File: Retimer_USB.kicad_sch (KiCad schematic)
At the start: 16 parts, among them IC1 PI2EQX22024XEAEX

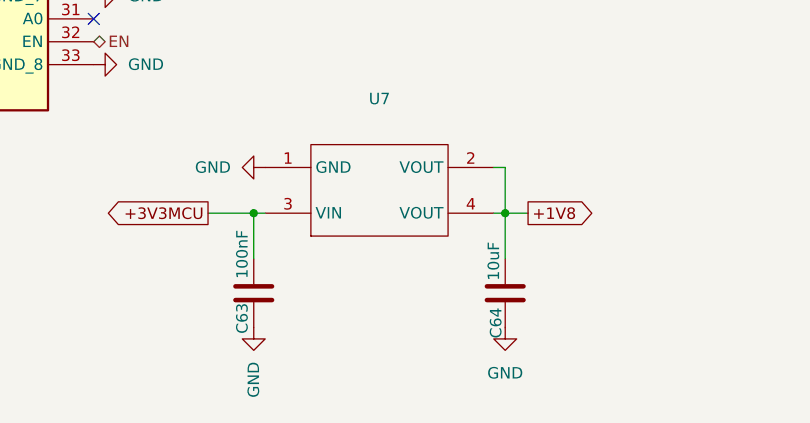
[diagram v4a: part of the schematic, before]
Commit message: added proper capacitators for ldo
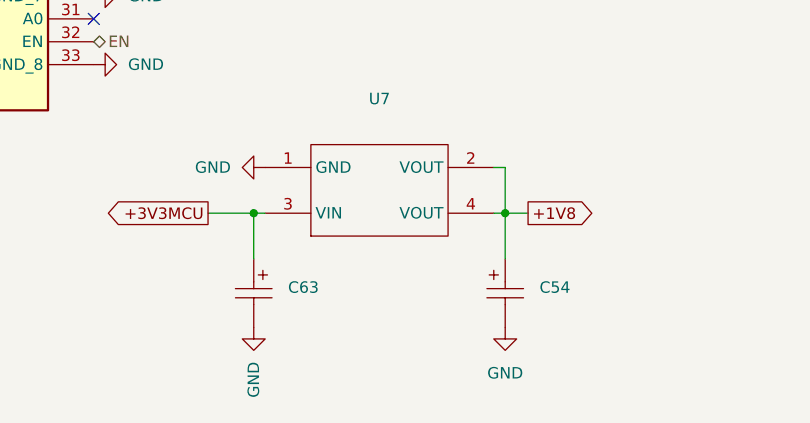
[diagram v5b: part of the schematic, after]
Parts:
- removed C63: 100nF, Capacitor_SMD:C_0201_0603Metric, symbol Device:C
- removed C64: 10uF, Capacitor_SMD:C_0603_1608Metric, symbol Device:C
- added C54: 10uF, TAJA106K016RNJ:CAP-SMD_L3.2-W1.6-RD-C7171, symbol TAJA106K016RNJ:TAJA106K016RNJ
- added C63: 100nF, TAJA104K035RNJ:CASE-A_3216, symbol TAJA104K035RNJ:TAJA104K035RNJ
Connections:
- net +1V8: now also C54.1
- net +3V3MCU: now also C63.1
- net GND: now also C54.2, C63.2
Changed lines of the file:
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@@
+	)
+	(symbol
+		(lib_id "TAJA104K035RNJ:TAJA104K035RNJ")
+		(at 198.12 133.35 270)
+		(unit 1)
+		(exclude_from_sim no)
+		(in_bom yes)
+		(on_board yes)
+		(dnp no)
+		(fields_autoplaced yes)
+		(property "Reference" "C63"
+			(at 201.93 132.7149 90)
+			(effects
+				(font
+					(size 1.27 1.27)
+				)
+				(justify left)
+			)
+		)
+		(property "Value" "100nF"
+			(at 198.12 133.35 0)
+			(effects
+				(font
+					(size 1.27 1.27)
+				)
+				(hide yes)
+			)
+		)
+		(property "Footprint" "TAJA104K035RNJ:CASE-A_3216"
+			(at 198.12 133.35 0)
+			(effects
+				(font
+					(size 1.27 1.27)
+				)
+				(hide yes)
+			)
+		)
+		(property "Datasheet" "https://atta.szlcsc.com/upload/public/pdf/source/20160107/1457707750344.pdf"
+			(at 198.12 133.35 0)
+			(effects
+				(font
+					(size 1.27 1.27)
+				)
+				(hide yes)
+			)
+		)
+		(property "Description" "Capacitance: Tolerance:±10% Tolerance:±10% Rated Voltage: Equivalent Series Resistance(ESR):24Ω@100kHz Operating Temperature:-55°C~+125°C Operating Temperature:-55°C~+125°C"
+			(at 198.12 133.35 0)
+			(effects
+				(font
+					(size 1.27 1.27)
+				)
+				(hide yes)
+			)
+		)
+		(property "Part_Number" "TAJA104K035RNJ"
+			(at 198.12 133.35 0)
+			(effects
+				(font
+					(size 1.27 1.27)
+				)
+				(hide yes)
+			)
+		)
+		(property "LCSC" "C7173"
+			(at 198.12 133.35 0)
+			(effects
+				(font
+					(size 1.27 1.27)
+				)
+				(hide yes)
+			)
+		)
+		(pin "1"
+		)
+		(pin "2"
+		)
+		(instances
+			(project ""
+				(path "/f97e6956-ab08-42cb-8fed-03fa58e87f0e/a254375d-80c0-4b18-9fd6-3cbd6a868414"
+					(reference "C63")
+					(unit 1)
+				)
+			)
+		)
 	)
 	(symbol
@@
 	)
 	(symbol
+		(lib_id "TAJA106K016RNJ:TAJA106K016RNJ")
+		(at 226.06 133.35 90)
+		(unit 1)
+		(exclude_from_sim no)
+		(in_bom yes)
+		(on_board yes)
+		(dnp no)
+		(fields_autoplaced yes)
+		(property "Reference" "C54"
+			(at 229.87 132.7149 90)
+			(effects
+				(font
+					(size 1.27 1.27)
+				)
+				(justify right)
+			)
+		)
+		(property "Value" "10uF"
+			(at 226.06 133.35 0)
+			(effects
+				(font
+					(size 1.27 1.27)
+				)
+				(hide yes)
+			)
+		)
+		(property "Footprint" "TAJA106K016RNJ:CAP-SMD_L3.2-W1.6-RD-C7171"
+			(at 226.06 133.35 0)
+			(effects
+				(font
+					(size 1.27 1.27)
+				)
+				(hide yes)
+			)
+		)
+		(property "Datasheet" ""
+			(at 226.06 133.35 0)
+			(effects
+				(font
+					(size 1.27 1.27)
+				)
+				(hide yes)
+			)
+		)
+		(property "Description" "Capacitance:10uF Tolerance:±10% Tolerance:±10% Voltage Rating:16V Equivalent Series Resistance(ESR):3Ω@100kHz Operating Temperature:-55°C~+125°C Operating Temperature:-55°C~+125°C"
+			(at 226.06 133.35 0)
+			(effects
+				(font
+					(size 1.27 1.27)
+				)
+				(hide yes)
+			)
+		)
+		(property "Part_Number" "TAJA106K016RNJ"
+			(at 226.06 133.35 0)
+			(effects
+				(font
+					(size 1.27 1.27)
+				)
+				(hide yes)
+			)
+		)
+		(property "Manufacturer" "Kyocera AVX"
+			(at 226.06 133.35 0)
+			(effects
+				(font
+					(size 1.27 1.27)
+				)
+				(hide yes)
+			)
+		)
+		(property "LCSC" "C7171"
+			(at 226.06 133.35 0)
+			(effects
+				(font
+					(size 1.27 1.27)
+				)
+				(hide yes)
+			)
+		)
+		(pin "1"
+		)
+		(pin "2"
+		)
+		(instances
+			(project "XG_Mobile_Dock_XT"
+				(path "/f97e6956-ab08-42cb-8fed-03fa58e87f0e/a254375d-80c0-4b18-9fd6-3cbd6a868414"
+					(reference "C54")
+					(unit 1)
+				)
+			)
+		)
+	)
+	(symbol
 		(lib_id "Device:C")
 		(at 114.3 90.17 270)
@@
 	)
 	(symbol
-		(lib_id "Device:C")
-		(at 226.06 133.35 0)
-		(mirror x)
-		(unit 1)
-		(exclude_from_sim no)
-		(in_bom yes)
-		(on_board yes)
-		(dnp no)
-		(property "Reference" "C64"
-			(at 225.044 136.652 90)
-			(effects
-				(font
-					(size 1.27 1.27)
-				)
-			)
-		)
-		(property "Value" "10uF"
-			(at 224.79 129.794 90)
-			(effects
-				(font
-					(size 1.27 1.27)
-				)
-			)
-		)
-		(property "Footprint" "Capacitor_SMD:C_0603_1608Metric"
-			(at 227.0252 129.54 0)
-			(effects
-				(font
-					(size 1.27 1.27)
-				)
-				(hide yes)
-			)
-		)
-		(property "Datasheet" "~"
-			(at 226.06 133.35 0)
-			(effects
-				(font
-					(size 1.27 1.27)
-				)
-				(hide yes)
-			)
-		)
-		(property "Description" "Unpolarized capacitor"
-			(at 226.06 133.35 0)
-			(effects
-				(font
-					(size 1.27 1.27)
-				)
-				(hide yes)
-			)
-		)
-		(property "Part_Number" "CL10A106KP8NNNC"
-			(at 226.06 133.35 0)
-			(effects
-				(font
-					(size 1.27 1.27)
-				)
-				(hide yes)
-			)
-		)
-		(property "LCSC" "C19702"
-			(at 226.06 133.35 0)
-			(effects
-				(font
-					(size 1.27 1.27)
-				)
-				(hide yes)
-			)
-		)
-		(pin "1"
-		)
-		(pin "2"
-		)
-		(instances
-			(project "XG_Mobile_Dock_XT"
-				(path "/f97e6956-ab08-42cb-8fed-03fa58e87f0e/a254375d-80c0-4b18-9fd6-3cbd6a868414"
-					(reference "C64")
-					(unit 1)
-				)
-			)
-		)
-	)
-	(symbol
 		(lib_id "power:GND")
 		(at 210.82 59.69 0)
@@
 					(unit 1)
 				)
-			)
-		)
-	)
-	(symbol
-		(lib_id "Device:C")
-		(at 198.12 133.35 0)
-		(unit 1)
-		(exclude_from_sim no)
-		(in_bom yes)
-		(on_board yes)
-		(dnp no)
-		(property "Reference" "C63"
-			(at 196.85 136.144 90)
-			(effects
-				(font
-					(size 1.27 1.27)
-				)
-			)
-		)
-		(property "Value" "100nF"
-			(at 196.85 129.032 90)
-			(effects
-				(font
-					(size 1.27 1.27)
-				)
-			)
-		)
-		(property "Footprint" "Capacitor_SMD:C_0201_0603Metric"
-			(at 199.0852 137.16 0)
-			(effects
-				(font
-					(size 1.27 1.27)
-				)
-				(hide yes)
-			)
-		)
-		(property "Datasheet" "~"
-			(at 198.12 133.35 0)
-			(effects
-				(font
-					(size 1.27 1.27)
-				)
-				(hide yes)
-			)
-		)
-		(property "Description" "Unpolarized capacitor"
-			(at 198.12 133.35 0)
-			(effects
-				(font
-					(size 1.27 1.27)
-				)
-				(hide yes)
-			)
-		)
-		(property "Part_Number" "GRM033R61C104KE84D"
-			(at 198.12 133.35 0)
-			(effects
-				(font
-					(size 1.27 1.27)
-				)
-				(hide yes)
-			)
-		)
-		(property "LCSC" "C76937"
-			(at 198.12 133.35 0)
-			(effects
-				(font
-					(size 1.27 1.27)
-				)
-				(hide yes)
-			)
-		)
-		(pin "1"
-		)
-		(pin "2"
-		)
-		(instances
-			(project "XG_Mobile_Dock_XT"
-				(path "/f97e6956-ab08-42cb-8fed-03fa58e87f0e/a254375d-80c0-4b18-9fd6-3cbd6a868414"
-					(reference "C63")
-					(unit 1)
-				)

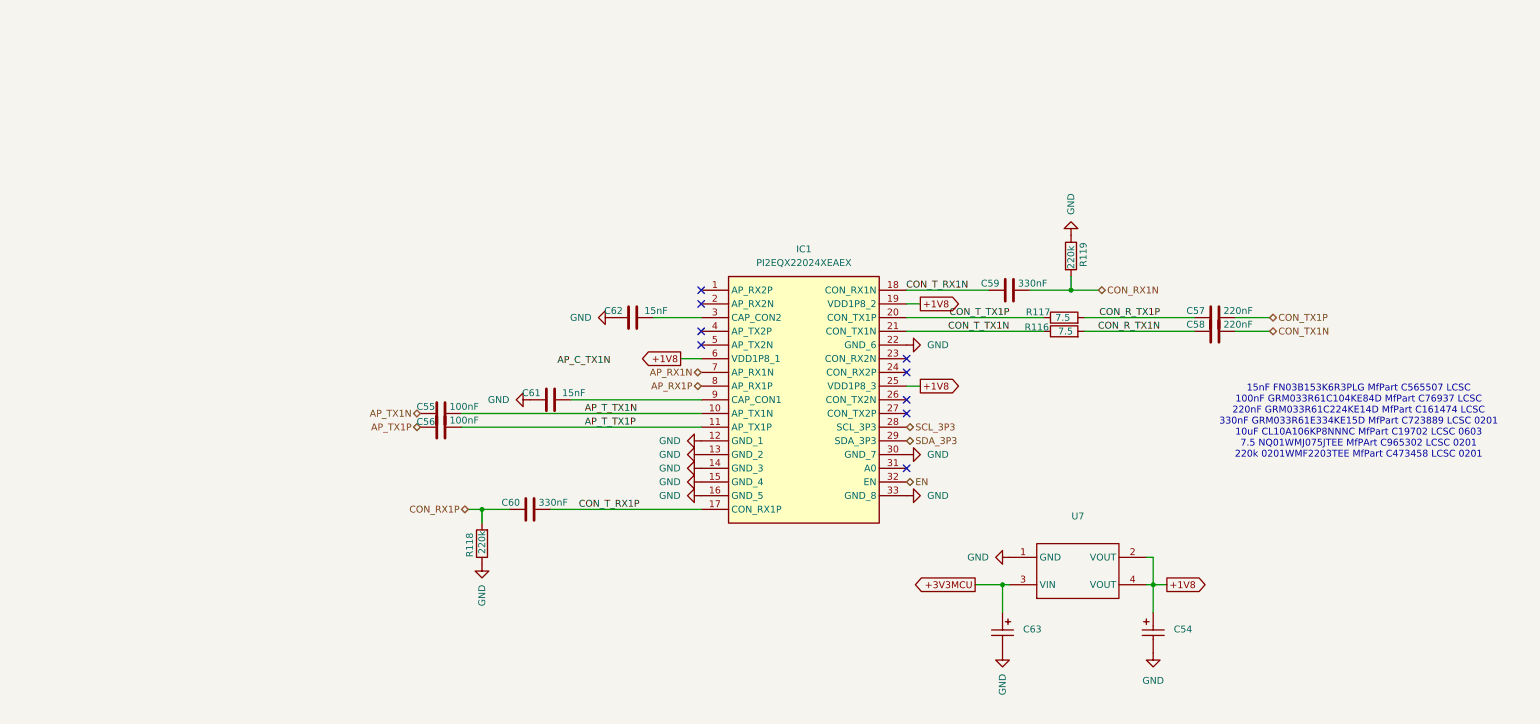
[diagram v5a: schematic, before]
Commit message: added more capacitators for usb retimer
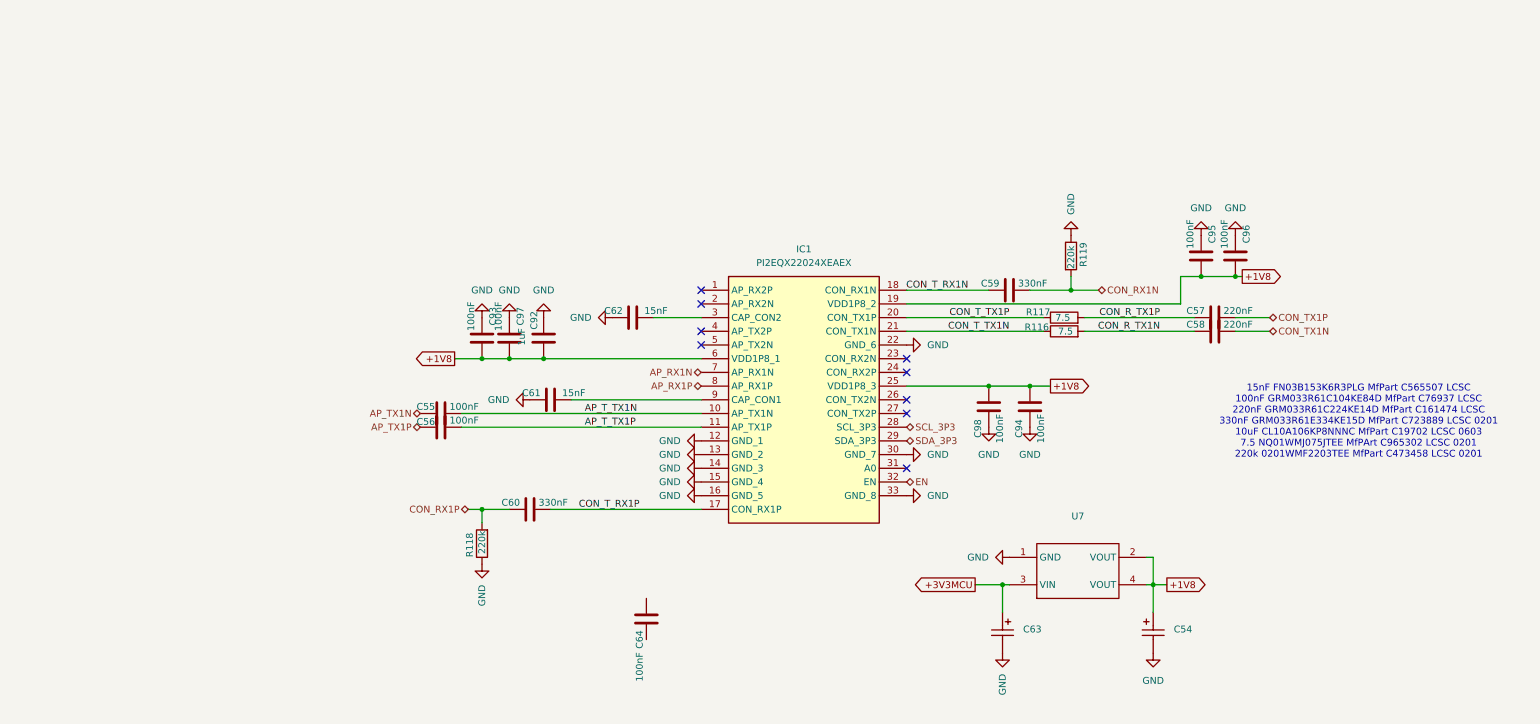
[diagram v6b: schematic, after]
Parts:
- added C64, C93, C94, C95, C96, C97, C98: 100nF, Capacitor_SMD:C_0201_0603Metric, symbol Device:C
- added C92: 1uF, Capacitor_SMD:C_0201_0603Metric, symbol Device:C
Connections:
- net +1V8: now also C92.2, C93.1, C94.1, C95.1, C96.1, C97.1, C98.1
- net GND: now also C92.1, C93.2, C94.2, C95.2, C96.2, C97.2, C98.2

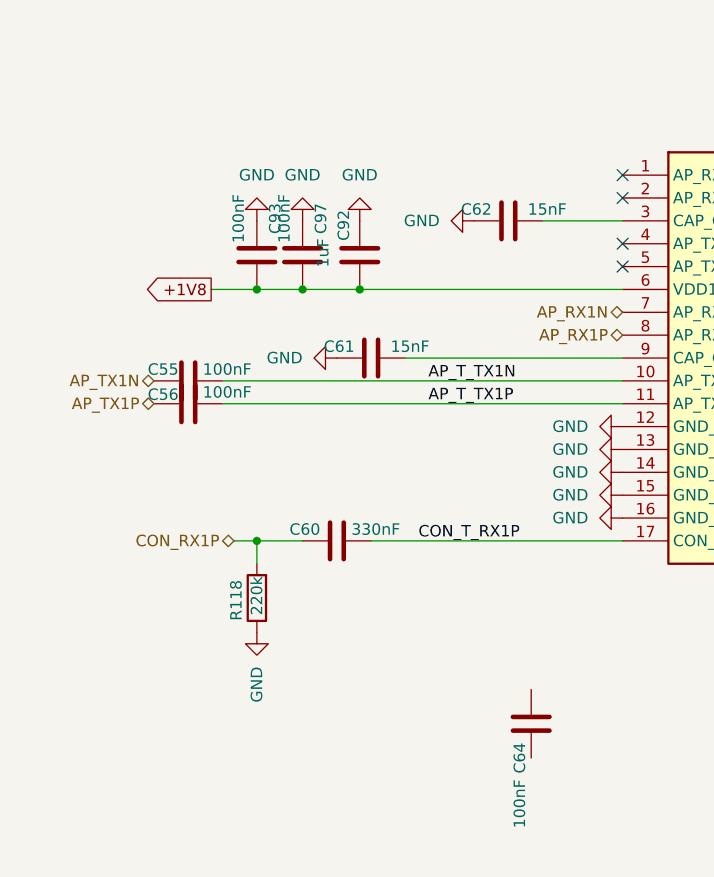
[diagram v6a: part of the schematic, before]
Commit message: added proper 10uF cap for usb retimer
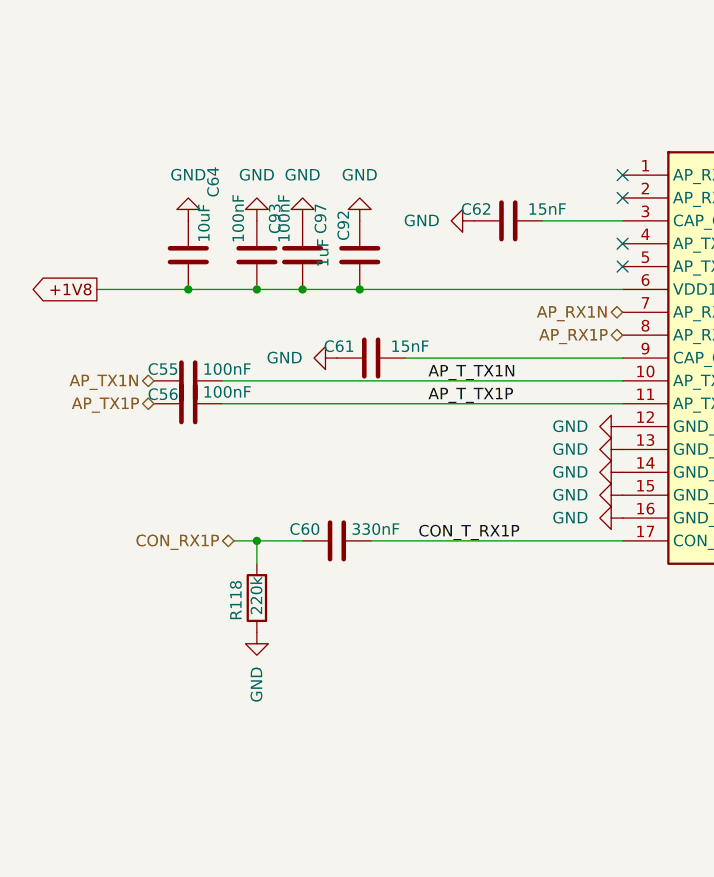
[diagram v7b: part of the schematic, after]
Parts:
- C64: value 100nF -> 10uF; footprint Capacitor_SMD:C_0201_0603Metric -> Capacitor_SMD:C_1206_3216Metric; LCSC C76937 -> C14860; Part_Number GRM033R61C104KE84D -> CL31B106KAHNNNE
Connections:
- net +1V8: now also C64.2
- net GND: now also C64.1
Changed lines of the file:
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@@
 	)
 	(junction
+		(at 93.98 82.55)
+		(diameter 0)
+		(color 0 0 0 0)
+	)
+	(junction
 		(at 195.58 87.63)
 		(diameter 0)
@@
 	(wire
 		(pts
-			(xy 96.52 82.55) (xy 101.6 82.55)
+			(xy 83.82 82.55) (xy 93.98 82.55)
 		)
 		(stroke
@@
 	(wire
 		(pts
+			(xy 93.98 82.55) (xy 101.6 82.55)
+		)
+		(stroke
+			(width 0)
+			(type default)
+		)
+	)
+	(wire
+		(pts
 			(xy 203.2 69.85) (xy 210.82 69.85)
 		)
@@
 	(global_label "+1V8"
 		(shape output)
-		(at 96.52 82.55 180)
+		(at 83.82 82.55 180)
 		(fields_autoplaced yes)
 		(effects
@@
 		)
 		(property "Intersheetrefs" "${INTERSHEET_REFS}"
-			(at 88.4548 82.55 0)
+			(at 75.7548 82.55 0)
 			(effects
 				(font
@@
 	)
 	(symbol
-		(lib_id "Device:C")
-		(at 132.08 130.81 0)
-		(mirror x)
-		(unit 1)
-		(exclude_from_sim no)
-		(in_bom yes)
-		(on_board yes)
-		(dnp no)
-		(property "Reference" "C64"
-			(at 130.81 134.62 90)
-			(effects
-				(font
-					(size 1.27 1.27)
-				)
-			)
-		)
-		(property "Value" "100nF"
-			(at 130.81 139.7 90)
-			(effects
-				(font
-					(size 1.27 1.27)
-				)
-			)
-		)
-		(property "Footprint" "Capacitor_SMD:C_0201_0603Metric"
-			(at 133.0452 127 0)
-			(effects
-				(font
-					(size 1.27 1.27)
-				)
-				(hide yes)
-			)
-		)
-		(property "Datasheet" "~"
-			(at 132.08 130.81 0)
-			(effects
-				(font
-					(size 1.27 1.27)
-				)
-				(hide yes)
-			)
-		)
-		(property "Description" "Unpolarized capacitor"
-			(at 132.08 130.81 0)
-			(effects
-				(font
-					(size 1.27 1.27)
-				)
-				(hide yes)
-			)
-		)
-		(property "Part_Number" "GRM033R61C104KE84D"
-			(at 132.08 130.81 0)
-			(effects
-				(font
-					(size 1.27 1.27)
-				)
-				(hide yes)
-			)
-		)
-		(property "LCSC" "C76937"
-			(at 132.08 130.81 0)
-			(effects
-				(font
-					(size 1.27 1.27)
-				)
-				(hide yes)
-			)
-		)
-		(pin "1"
-		)
-		(pin "2"
-		)
-		(instances
-			(project "XG_Mobile_Dock_XT"
-				(path "/f97e6956-ab08-42cb-8fed-03fa58e87f0e/a254375d-80c0-4b18-9fd6-3cbd6a868414"
-					(reference "C64")
-					(unit 1)
-				)
-			)
-		)
-	)
-	(symbol
 		(lib_id "Device:R")
 		(at 101.6 116.84 180)
@@
 	)
 	(symbol
+		(lib_id "Device:C")
+		(at 93.98 78.74 0)
+		(mirror y)
+		(unit 1)
+		(exclude_from_sim no)
+		(in_bom yes)
+		(on_board yes)
+		(dnp no)
+		(property "Reference" "C64"
+			(at 96.774 70.612 90)
+			(effects
+				(font
+					(size 1.27 1.27)
+				)
+			)
+		)
+		(property "Value" "10uF"
+			(at 95.758 75.184 90)
+			(effects
+				(font
+					(size 1.27 1.27)
+				)
+			)
+		)
+		(property "Footprint" "Capacitor_SMD:C_1206_3216Metric"
+			(at 93.0148 82.55 0)
+			(effects
+				(font
+					(size 1.27 1.27)
+				)
+				(hide yes)
+			)
+		)
+		(property "Datasheet" "~"
+			(at 93.98 78.74 0)
+			(effects
+				(font
+					(size 1.27 1.27)
+				)
+				(hide yes)
+			)
+		)
+		(property "Description" "Unpolarized capacitor"
+			(at 93.98 78.74 0)
+			(effects
+				(font
+					(size 1.27 1.27)
+				)
+				(hide yes)
+			)
+		)
+		(property "Part_Number" "CL31B106KAHNNNE"
+			(at 93.98 78.74 0)
+			(effects
+				(font
+					(size 1.27 1.27)
+				)
+				(hide yes)
+			)
+		)
+		(property "LCSC" "C14860"
+			(at 93.98 78.74 0)
+			(effects
+				(font
+					(size 1.27 1.27)
+				)
+				(hide yes)
+			)
+		)
+		(pin "1"
+		)
+		(pin "2"
+		)
+		(instances
+			(project "XG_Mobile_Dock_XT"
+				(path "/f97e6956-ab08-42cb-8fed-03fa58e87f0e/a254375d-80c0-4b18-9fd6-3cbd6a868414"
+					(reference "C64")
+					(unit 1)
+				)
+			)
+		)
+	)
+	(symbol
 		(lib_id "power:GND")
 		(at 180.34 100.33 90)
@@
 					(unit 1)
 				)
+			)
+		)
+	)
+	(symbol
+		(lib_id "power:GND")
+		(at 93.98 74.93 180)
+		(unit 1)
+		(exclude_from_sim no)
+		(in_bom yes)
+		(on_board yes)
+		(dnp no)
+		(fields_autoplaced yes)
+		(property "Reference" "#PWR0192"
+			(at 93.98 68.58 0)
+			(effects
+				(font
+					(size 1.27 1.27)
+				)
+				(hide yes)
+			)
+		)
+		(property "Value" "GND"
+			(at 93.98 69.85 0)
+			(effects
+				(font
+					(size 1.27 1.27)
+				)
+			)
+		)
+		(property "Footprint" ""
+			(at 93.98 74.93 0)
+			(effects
+				(font
+					(size 1.27 1.27)
+				)
+				(hide yes)
+			)
+		)
+		(property "Datasheet" ""
+			(at 93.98 74.93 0)
+			(effects
+				(font
+					(size 1.27 1.27)
+				)
+				(hide yes)
+			)
+		)
+		(property "Description" "Power symbol creates a global label with name \"GND\" , ground"
+			(at 93.98 74.93 0)
+			(effects
+				(font
+					(size 1.27 1.27)
+				)
+				(hide yes)
+			)
+		)
+		(pin "1"
+		)
+		(instances
+			(project "XG_Mobile_Dock_XT"
+				(path "/f97e6956-ab08-42cb-8fed-03fa58e87f0e/a254375d-80c0-4b18-9fd6-3cbd6a868414"
+					(reference "#PWR0192")
+					(unit 1)
+				)
